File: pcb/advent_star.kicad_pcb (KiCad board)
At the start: 2 copper layers, 69.6 x 69.6 mm, 106 parts, among them J1 TC2030, Q1 AO3401A, SW1 SW_Push_Dual, U1 CH32V003FxUx, U2 SC7A20

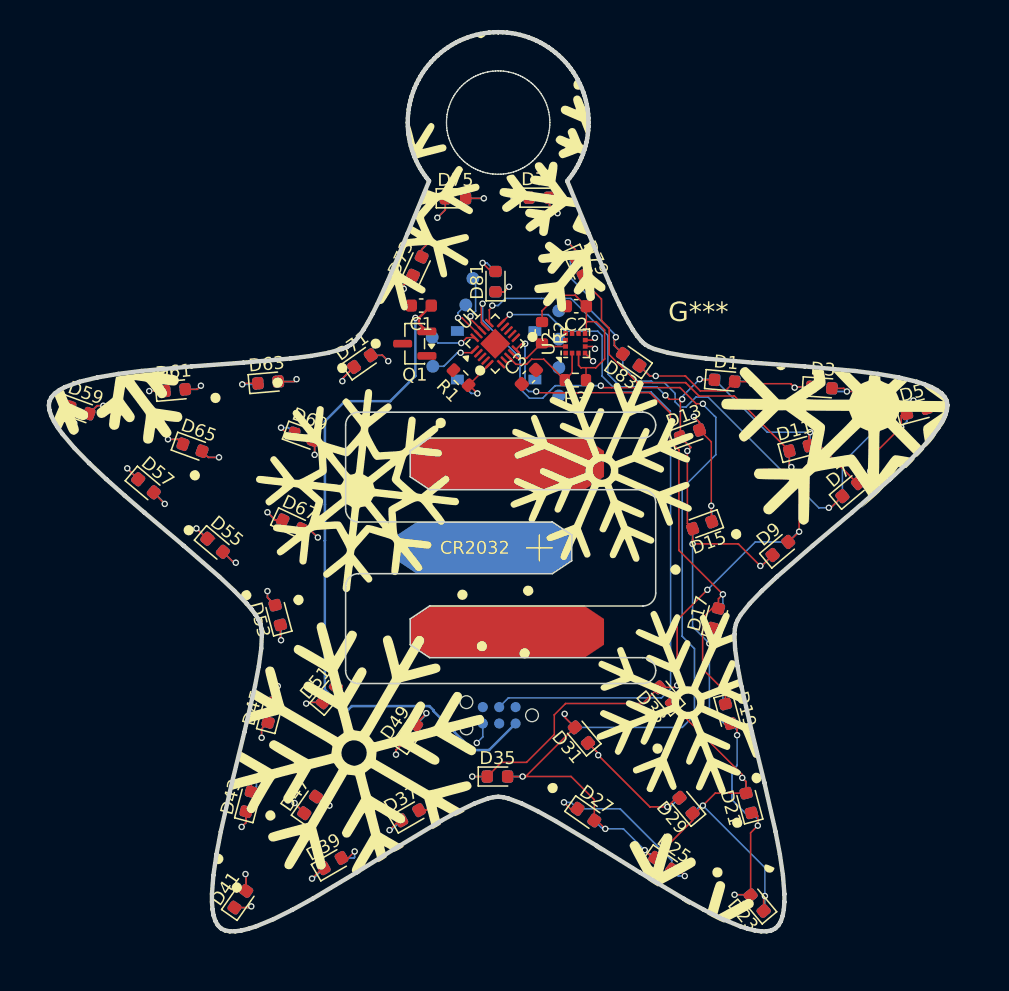
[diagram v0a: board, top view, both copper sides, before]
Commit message: charlieplex matrix finished, WIP on routing microcontroller
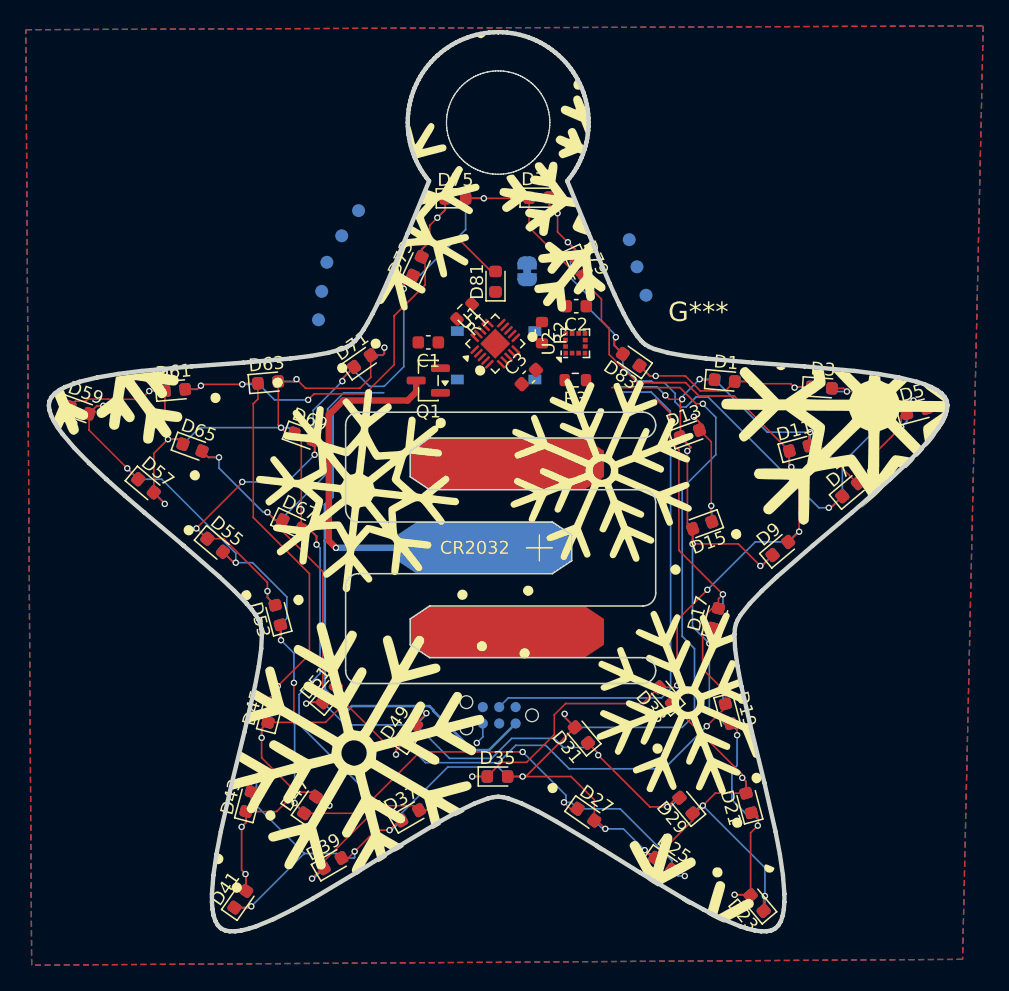
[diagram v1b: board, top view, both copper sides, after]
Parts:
- removed TP6: TestPoint_Small, TestPoint:TestPoint_Pad_D1.0mm
- added JP1: SolderJumper_2_Bridged, Jumper:SolderJumper-2_P1.3mm_Bridged_RoundedPad1.0x1.5mm, B.Cu at (152.3, 81.8)
- added TP9: TestPoint_Small, TestPoint:TestPoint_Pad_D1.0mm, B.Cu at (160.2, 79.4)
- moved TP1 21.1 mm to (139.3, 77.2)
- moved TP3 11.2 mm to (136.8, 81.2)
- moved TP2 10.7 mm to (138.0, 79.1)
- moved TP5 9.55 mm to (136.2, 85.6)
- moved TP4 9.26 mm to (136.4, 83.4)
- moved TP8 8.77 mm to (161.6, 83.7)
- moved TP7 8.24 mm to (160.8, 81.5)
- moved R1 5.14 mm to (147.5, 85.0), turned to -135 degrees
- moved Q1 3.04 mm to (144.7, 90.3)
- moved C1 2.90 mm to (144.7, 87.3)
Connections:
- TP1 pad 1: Net-(U1-PC0) -> Net-(U1-PD3)
- U1 pad 10: LED_C3 -> LED_C4
- U1 pad 11: LED_C4 -> Net-(U1-PC4)
- U1 pad 16: LED_C1 -> USER_BTN
- U1 pad 17: LED_C2 -> Net-(U1-PD3)
- U1 pad 5: USER_BTN -> SDA
- U1 pad 7: Net-(U1-PC0) -> LED_C1
- U1 pad 8: SDA -> LED_C2
- U1 pad 9: SCL -> LED_C3
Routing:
- net LED_C7: track 52.7 -> 142.3 mm, vias 12 -> 13
- net LED_C4: track 39.3 -> 116.3 mm, vias 12 -> 13
- net LED_C3: track 71.4 -> 143.6 mm
- net LED_C6: track 80.0 -> 139.8 mm, vias 12 -> 11
- net LED_C5: track 91.6 -> 144.4 mm, vias 13 -> 14
- net +BATT: track 0.00 -> 29.7 mm, vias 0 -> 1
- net VDD: track 70.2 -> 44.6 mm, vias 1 -> 0
- net LED_C1: track 121.4 -> 105.2 mm, vias 15 -> 14
- net SWIO: track 53.6 -> 40.0 mm, vias 1 -> 0
- net LED_C2: track 132.2 -> 143.8 mm, vias 15 -> 13
- net SDA: track 7.74 -> 0.00 mm
- net USER_BTN: track 5.23 -> 0.00 mm, vias 1 -> 0
- net SCL: track 4.86 -> 0.00 mm
- net Net-(U1-PD4): track 4.65 -> 0.00 mm, vias 1 -> 0
- net Net-(U1-PD7): track 3.78 -> 0.00 mm, vias 1 -> 0
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- added copper zone on B.Cu, net GND
- added copper zone on F.Cu, net GND

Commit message: almost done with routing, needs two ground pads to be connected
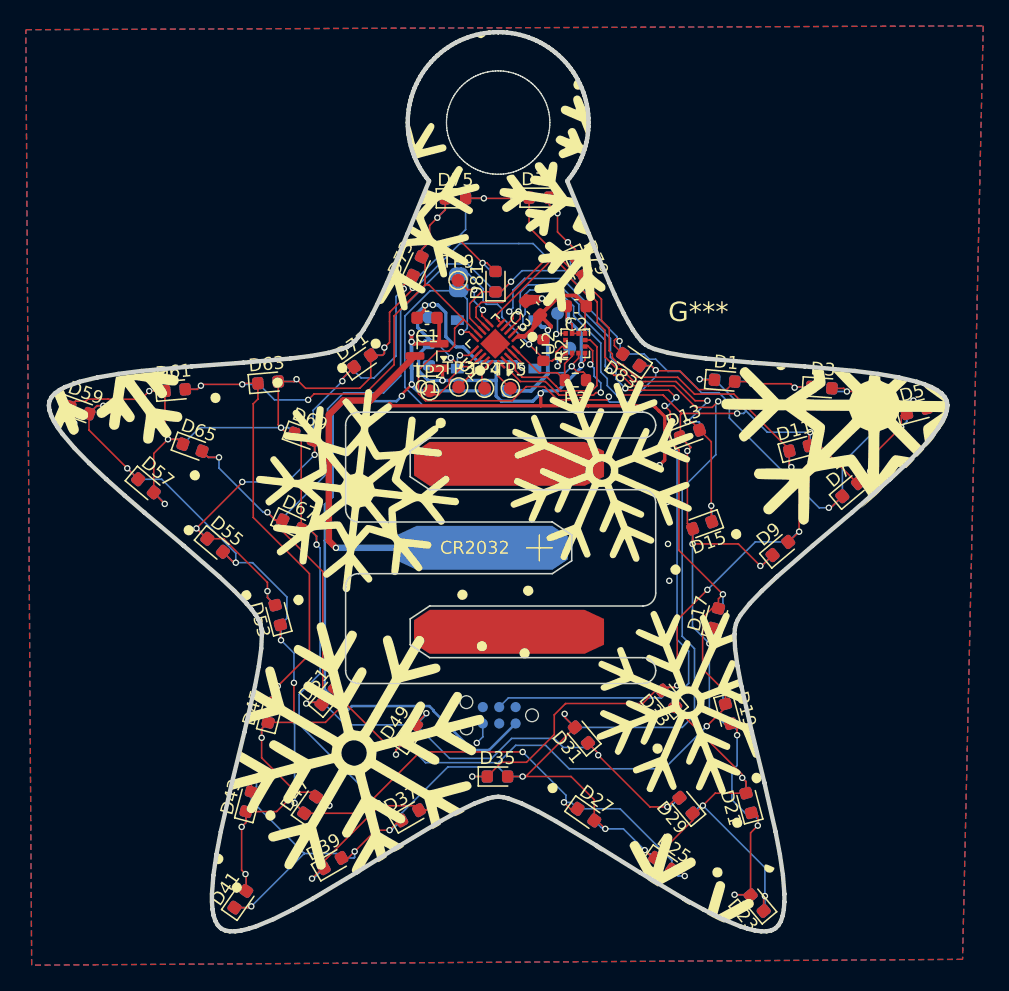
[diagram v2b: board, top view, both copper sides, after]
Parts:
- added R4: 0, Resistor_SMD:R_0603_1608Metric, B.Cu at (149.9, 91.1)
- R1: moved to B.Cu
- TP2, TP3, TP4, TP5, TP9: moved to F.Cu
- moved TP5 15.8 mm to (151.1, 90.9)
- moved TP4 14.7 mm to (149.1, 90.9)
- moved TP3 14.0 mm to (147.1, 90.8)
- moved TP2 13.8 mm to (144.8, 91.1)
- moved TP9 13.6 mm to (147.0, 82.5)
- moved TP1 9.86 mm to (144.7, 85.4)
- moved TP8 7.18 mm to (155.7, 87.8)
- moved TP7 7.13 mm to (154.7, 85.1)
- moved JP1 5.37 mm to (147.1, 82.7)
- moved C3 5.34 mm to (152.8, 84.7), turned to 135 degrees
- moved R1 4.33 mm to (144.8, 88.3), turned to 90 degrees
- moved C1 1.90 mm to (144.6, 85.5)
- moved Q1 1.90 mm to (144.6, 88.4)
- moved R2 1.35 mm to (153.6, 88.0)
- moved SW1 0.85 mm to (149.9, 87.5)
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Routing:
- net GND: track 1.70 -> 79.5 mm, vias 1 -> 14
- net LED_C4: track 116.3 -> 163.4 mm, vias 13 -> 16
- net VDD: track 44.6 -> 87.5 mm, vias 0 -> 6
- net LED_C7: track 142.3 -> 178.1 mm, vias 13 -> 15
- net SWIO: track 40.0 -> 73.4 mm, vias 0 -> 1
- net LED_C6: track 139.8 -> 168.6 mm, vias 11 -> 12
- net LED_C3: track 143.6 -> 166.2 mm, vias 14 -> 18
- net LED_C1: track 105.2 -> 123.8 mm, vias 14 -> 15
- net LED_C2: track 143.8 -> 160.8 mm, vias 13 -> 15
- net INT1: track 0.09 -> 13.4 mm, vias 0 -> 2
- net SCL: track 0.00 -> 12.8 mm, vias 0 -> 1
- net INT2: track 0.00 -> 12.5 mm
- net LED_C5: track 144.4 -> 154.2 mm
- net SDA: track 0.00 -> 7.11 mm
- net Net-(U1-PD3): track 0.00 -> 6.71 mm, vias 0 -> 1
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
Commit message: finished assignment of parts for jlcpcb, current state is ordered
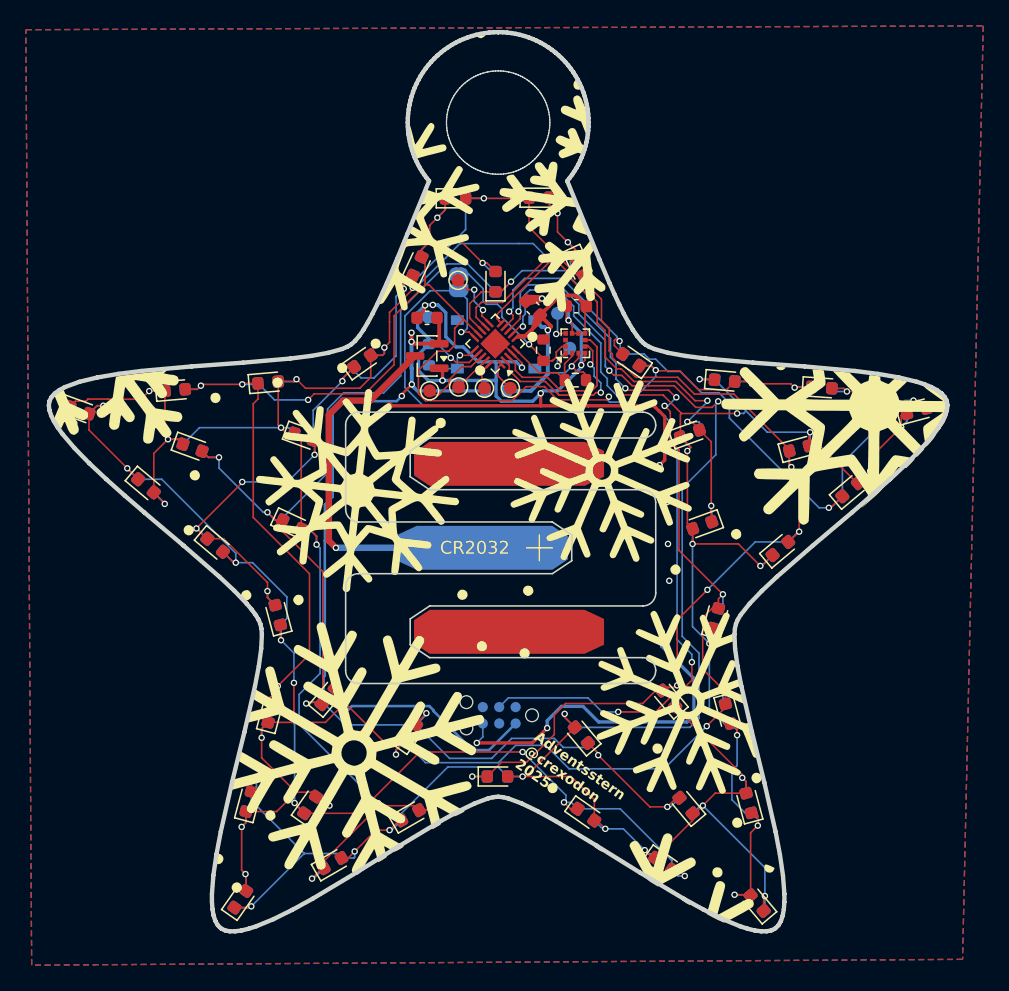
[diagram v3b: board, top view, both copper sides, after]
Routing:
- net GND: track 79.5 -> 106.1 mm, vias 14 -> 15
- net SWIO: track 73.4 -> 74.5 mm, vias 1 -> 3
- net LED_C2: track 160.8 -> 161.4 mm
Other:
- board text added: "Adventsstern @crexodon 2025"
